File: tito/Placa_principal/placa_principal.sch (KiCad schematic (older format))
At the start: 14 parts, among them IC1 ATMEGA8-P, P1 CONN_3X2, P2 CONN_3X2, P3 CONN_3X2

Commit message: Cambios minimos en la placa, se empezo con la generacion de la netlist.
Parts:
- removed P3: CONN_3X2, symbol CONN_3X2
- added P4: CONN_4X2, symbol CONN_4X2
- added P5, P6: CONN_2, symbol CONN_2
- added R7: 100, symbol R
- added R8: RVAR, symbol RVAR
- gave numbers to parts that had none: 3
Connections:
- net labels added: SENSOR_CURVA
- wire segments 75 -> 96
- no-connect marks 0 -> 6
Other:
- moved on the sheet: P1, P2, P3, R1, R2, R3, U1

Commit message: Cambiamos de regulador a un LDO de más corriente. Cambiamos algunos pines para facilitar el diseño del PCB.
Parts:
- removed R4, R5, R6, R8: RVAR, symbol RVAR
- removed U2: 7805, symbol 7805
- added RV1, RV2, RV3, RV4: POT, symbol POT
- added U?: REG_104-5, symbol REG_104-5
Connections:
- net labels added: +BATT
- net labels removed: BATT
- wire segments 96 -> 112
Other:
- moved on the sheet: P4, R1, R2, R3, R7

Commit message: Cambios a la placa, routeada pero con muchos cables y faltan algunas vias. Agregado magia de diodos para Puente-H.
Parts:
- added D1, D2, D3, D4, D5, D6, D7, D8: DIODE, symbol DIODE
- gave numbers to parts that had none: 1
- renumbered P5 to P1, P6 to P2, P4 to P3, P3 to P4, P1 to P5, P2 to P6, R7 to R4
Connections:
- net labels removed: VCC
- wire segments 112 -> 138
- no-connect marks 6 -> 7

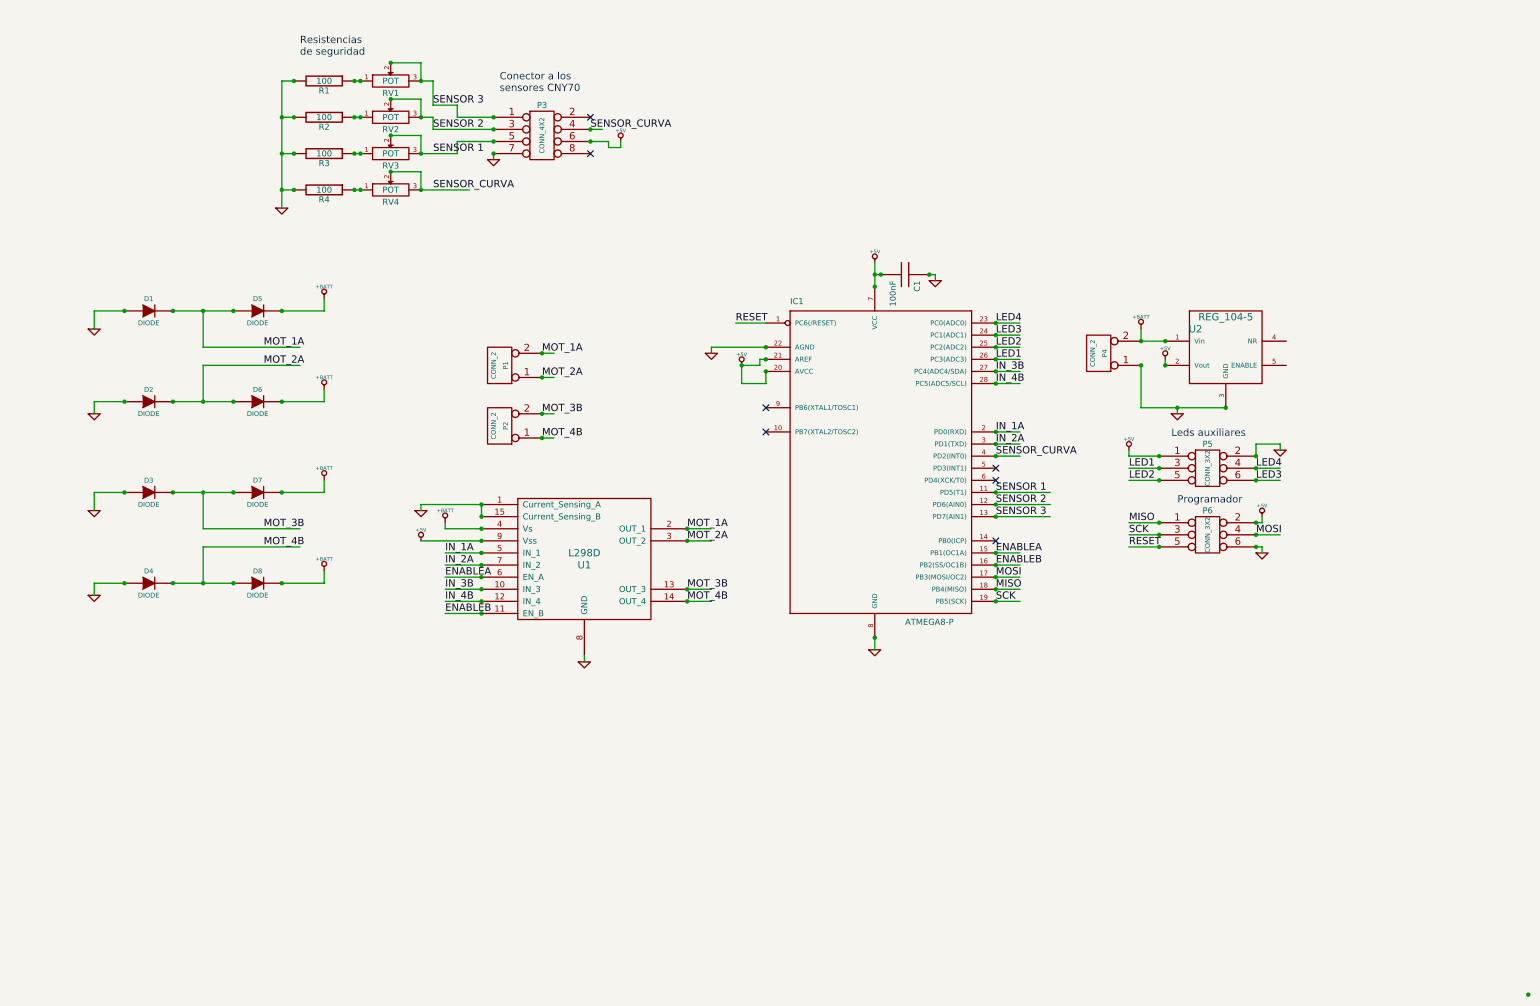
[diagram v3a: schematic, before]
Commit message: nuevo trabajo sobre el pcb, agregamos las especificaciones del regulador de tension, falta cambiar el encapsulado del mismo, agregar smd.
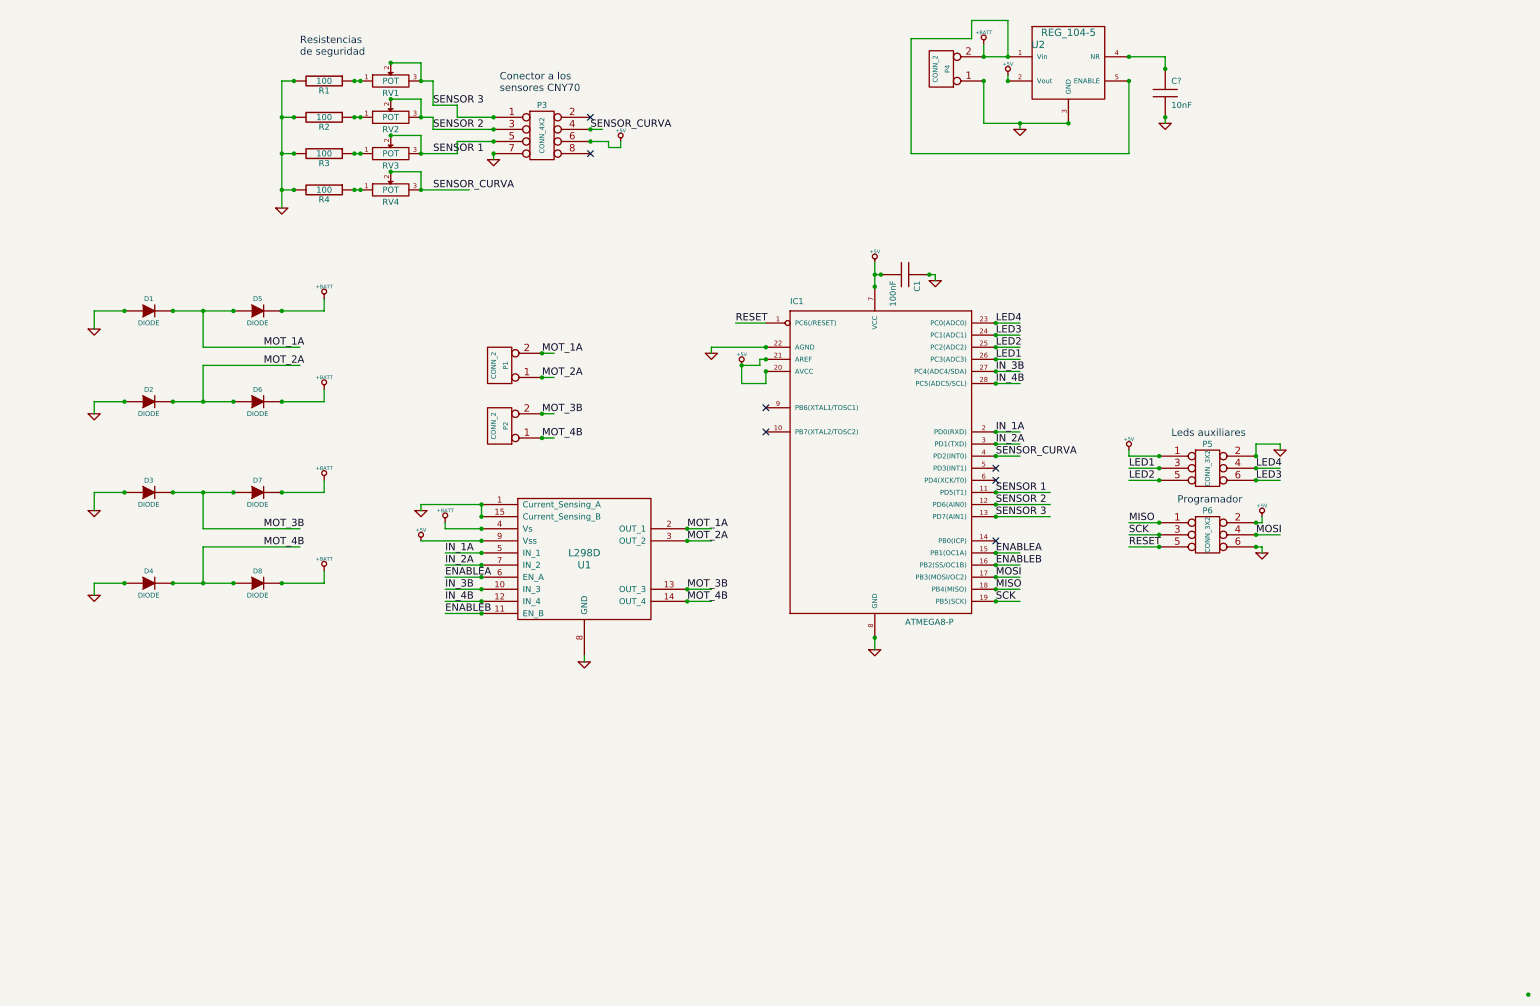
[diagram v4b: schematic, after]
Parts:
- added C?: 10nF, symbol C
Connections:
- wire segments 138 -> 148
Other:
- moved on the sheet: P4, U2

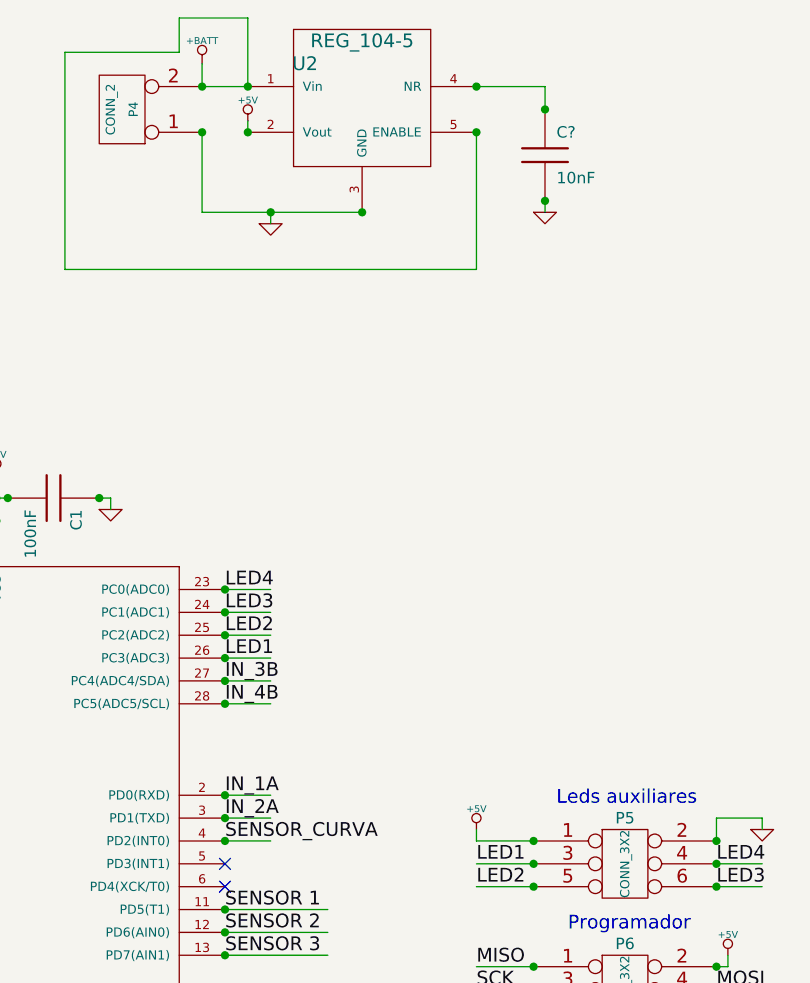
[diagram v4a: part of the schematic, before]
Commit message: agrego regulador de tension, y TERMINAMOS EL PCB!!!
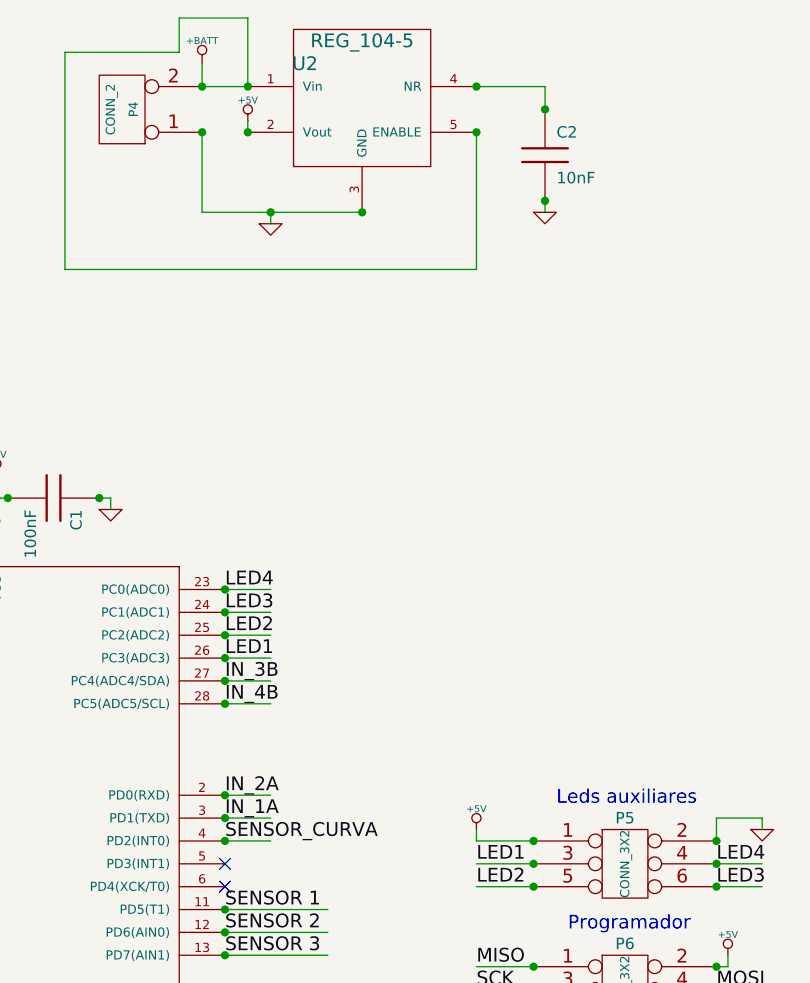
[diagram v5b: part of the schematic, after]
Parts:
- gave numbers to parts that had none: 1
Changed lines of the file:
@@
-EESchema Schematic File Version 2  date vie 27 may 2011 21:56:14 ART
+EESchema Schematic File Version 2  date vie 03 jun 2011 21:59:30 ART
 LIBS:power
 LIBS:device
@@
 Sheet 1 1
 Title "Tito, el autito más bonito"
-Date "28 may 2011"
+Date "4 jun 2011"
 Rev "0.3"
 Comp ""
@@
 Connection ~ 10050 1800
 $Comp
-L GND #PWR?
+L GND #PWR25
 U 1 1 4DE04806
 P 10050 1850
-F 0 "#PWR?" H 10050 1850 30  0001 C CNN
+F 0 "#PWR25" H 10050 1850 30  0001 C CNN
 F 1 "GND" H 10050 1780 30  0001 C CNN
 	1    10050 1850
@@
 	10050 1300 10050 1400
 $Comp
-L C C?
+L C C2
 U 1 1 4DE047FF
 P 10050 1600
-F 0 "C?" H 10100 1700 50  0000 L CNN
+F 0 "C2" H 10100 1700 50  0000 L CNN
 F 1 "10nF" H 10100 1500 50  0000 L CNN
 	1    10050 1600
@@
 NoConn ~ 5300 1800
 $Comp
-L +5V #PWR23
+L +5V #PWR22
 U 1 1 4DC499E2
 P 8750 1450
-F 0 "#PWR23" H 8750 1540 20  0001 C CNN
+F 0 "#PWR22" H 8750 1540 20  0001 C CNN
 F 1 "+5V" H 8750 1540 30  0000 C CNN
 	1    8750 1450
@@
 $EndComp
 $Comp
-L +BATT #PWR22
+L +BATT #PWR21
 U 1 1 4DC490C1
 P 8550 1200
-F 0 "#PWR22" H 8550 1150 20  0001 C CNN
+F 0 "#PWR21" H 8550 1150 20  0001 C CNN
 F 1 "+BATT" H 8550 1300 30  0000 C CNN
 	1    8550 1200
@@
 SENSOR_CURVA
 $Comp
-L GND #PWR24
+L GND #PWR23
 U 1 1 4DA8E53A
 P 8850 1900
-F 0 "#PWR24" H 8850 1900 30  0001 C CNN
+F 0 "#PWR23" H 8850 1900 30  0001 C CNN
 F 1 "GND" H 8850 1830 30  0001 C CNN
 	1    8850 1900
@@
 Text Label 8650 3900 0    60   ~ 0
 IN_3B
+Text Label 8650 4400 0    60   ~ 0
+IN_2A
 Text Label 8650 4500 0    60   ~ 0
-IN_2A
-Text Label 8650 4400 0    60   ~ 0
 IN_1A
 Text Label 8650 5400 0    60   ~ 0
@@
 MOSI
 $Comp
-L GND #PWR26
+L GND #PWR27
 U 1 1 4DA49E6B
 P 10850 5400
-F 0 "#PWR26" H 10850 5400 30  0001 C CNN
+F 0 "#PWR27" H 10850 5400 30  0001 C CNN
 F 1 "GND" H 10850 5330 30  0001 C CNN
 	1    10850 5400
@@
 $EndComp
 $Comp
-L +5V #PWR25
+L +5V #PWR26
 U 1 1 4DA49E66
 P 10850 5100
-F 0 "#PWR25" H 10850 5190 20  0001 C CNN
+F 0 "#PWR26" H 10850 5190 20  0001 C CNN
 F 1 "+5V" H 10850 5190 30  0000 C CNN
 	1    10850 5100
@@
 LED4
 $Comp
-L GND #PWR27
+L GND #PWR28
 U 1 1 4DA49C68
 P 11000 4550
-F 0 "#PWR27" H 11000 4550 30  0001 C CNN
+F 0 "#PWR28" H 11000 4550 30  0001 C CNN
 F 1 "GND" H 11000 4480 30  0001 C CNN
 	1    11000 4550
@@
 $EndComp
 $Comp
-L +5V #PWR21
+L +5V #PWR24
 U 1 1 4DA49C4D
 P 9750 4550
-F 0 "#PWR21" H 9750 4640 20  0001 C CNN
+F 0 "#PWR24" H 9750 4640 20  0001 C CNN
 F 1 "+5V" H 9750 4640 30  0000 C CNN
 	1    9750 4550

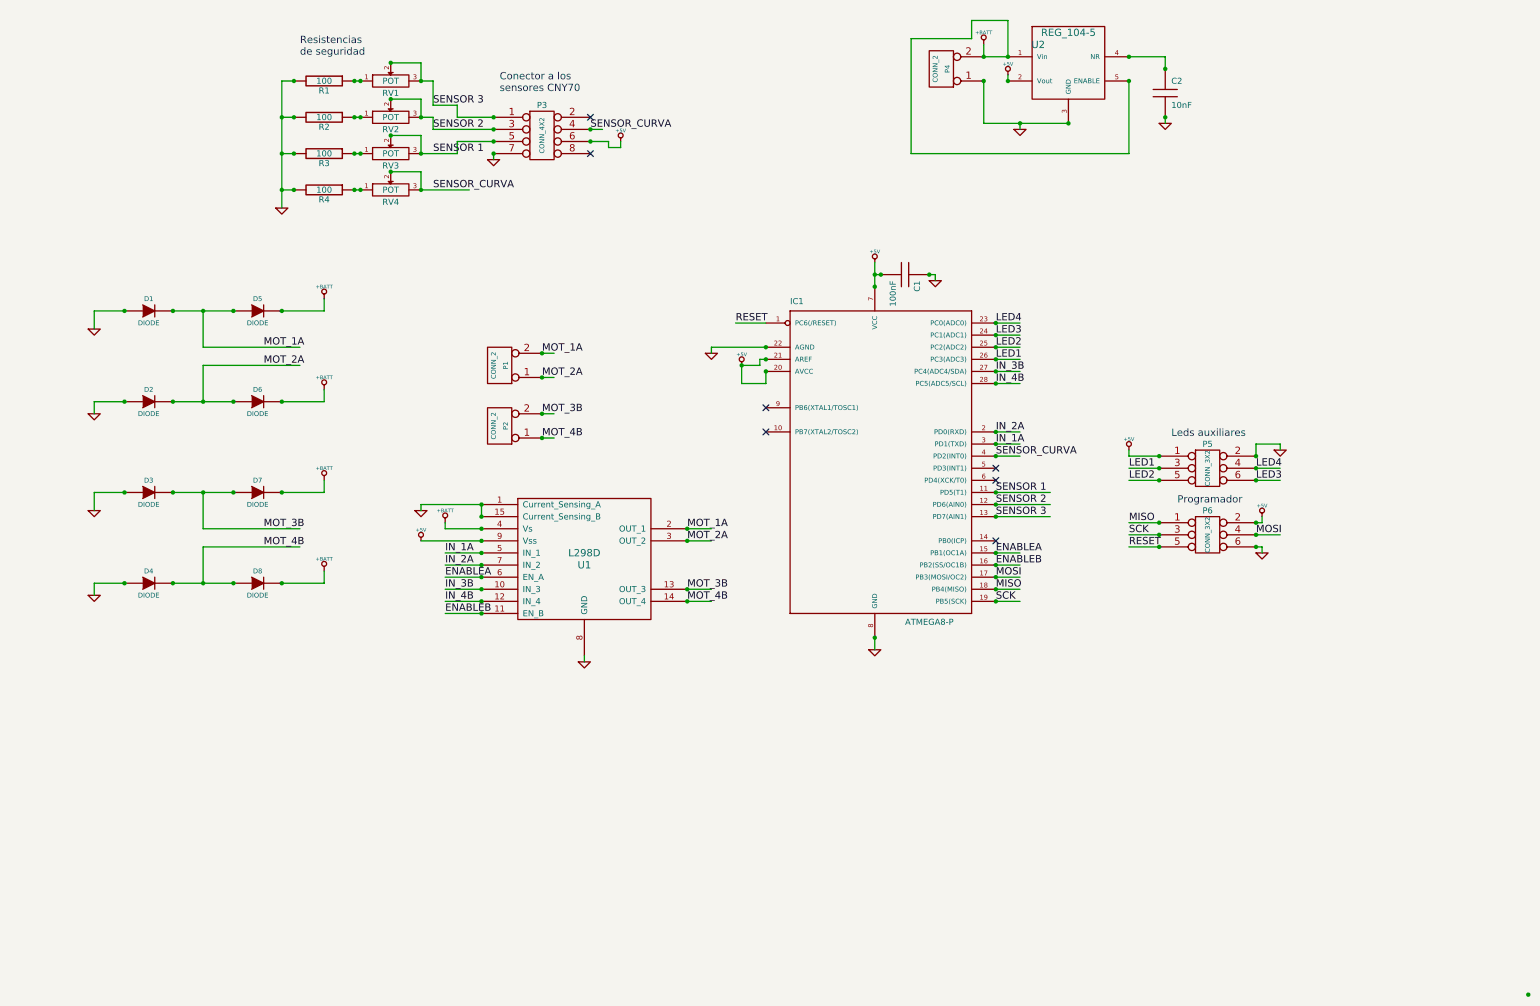
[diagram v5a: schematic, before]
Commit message: reestructure el pcb, y agregue el boton. ahora esta linda la placa
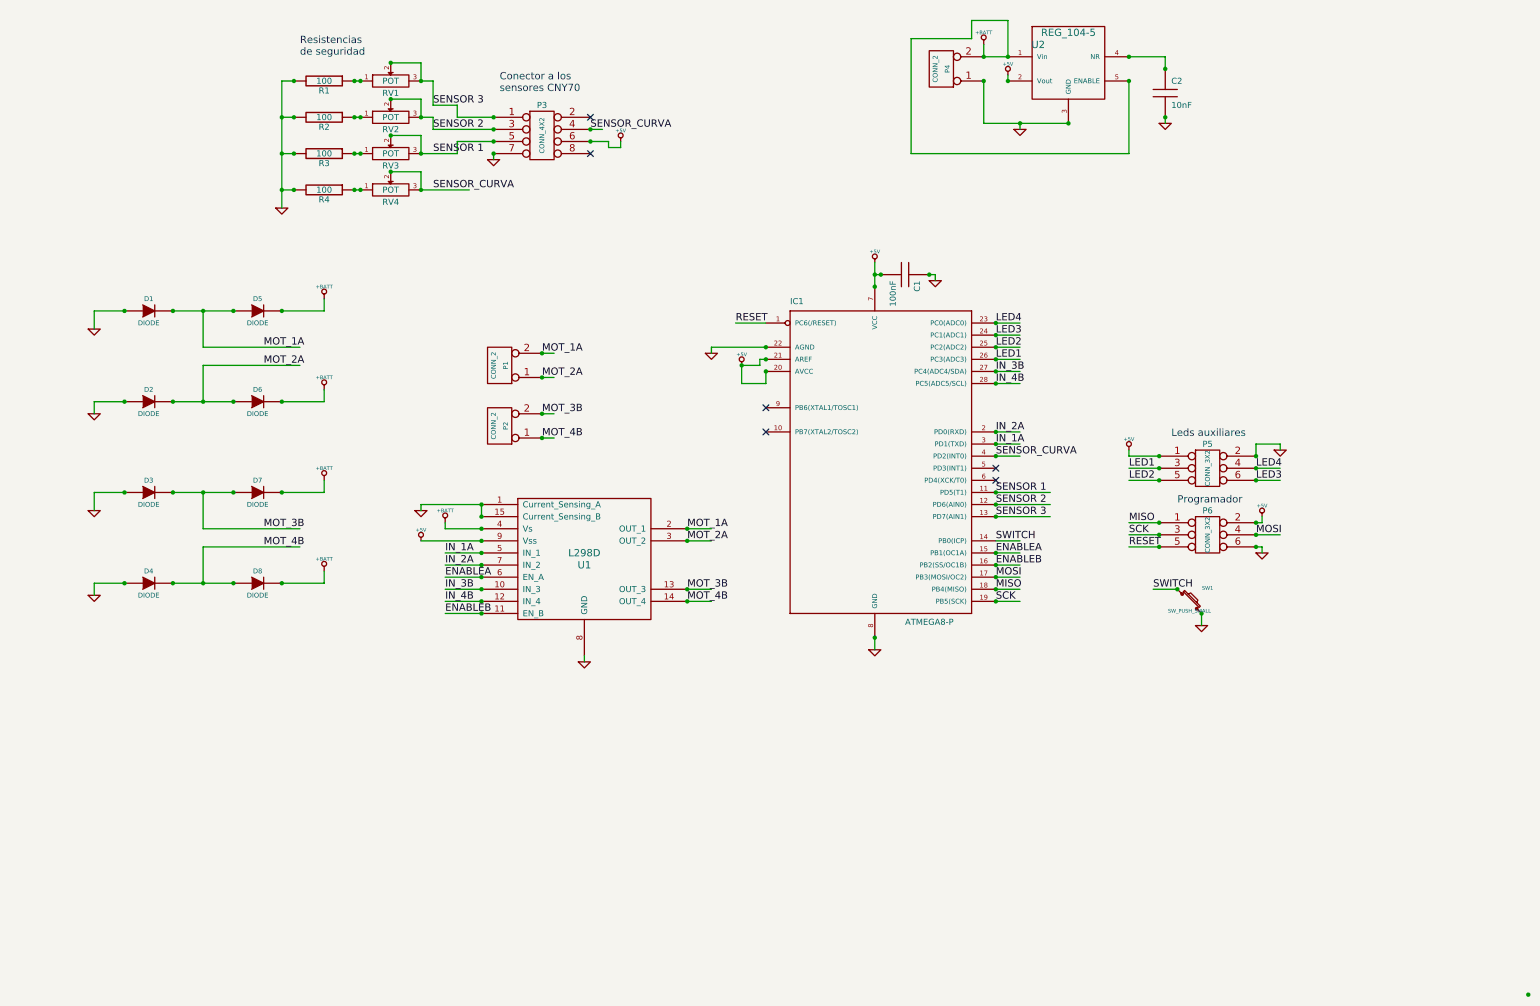
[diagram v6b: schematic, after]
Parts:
- added SW1: SW_PUSH_SMALL, symbol SW_PUSH_SMALL
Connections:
- net labels added: SWITCH
- wire segments 148 -> 151
- no-connect marks 7 -> 6
